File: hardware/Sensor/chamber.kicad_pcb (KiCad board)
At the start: 2 copper layers, 100 x 100 mm, 99 parts, among them J1 USB_B_Micro, J32 RF_Shield_Two_Pieces, J33 RF_Shield_Two_Pieces, J34 Conn_Coaxial, J51 Conn_02x05_Counter_Clockwise, J52 Conn_01x04, Q31 BC859, Q32 Q_NMOS_GDS, Q51 2N7002, Q52 Q_NPN_BEC, SW31 SW_DPDT_x2, SW32 SW_DPDT_x2, U31 MC34063AD, U32 LMC662, U33 LM358, U51 Opamp_Dual_Generic, U52 MCP3425A0T-ECH, U53 MCP3425A0T-ECH, U54 STM8S003F3P

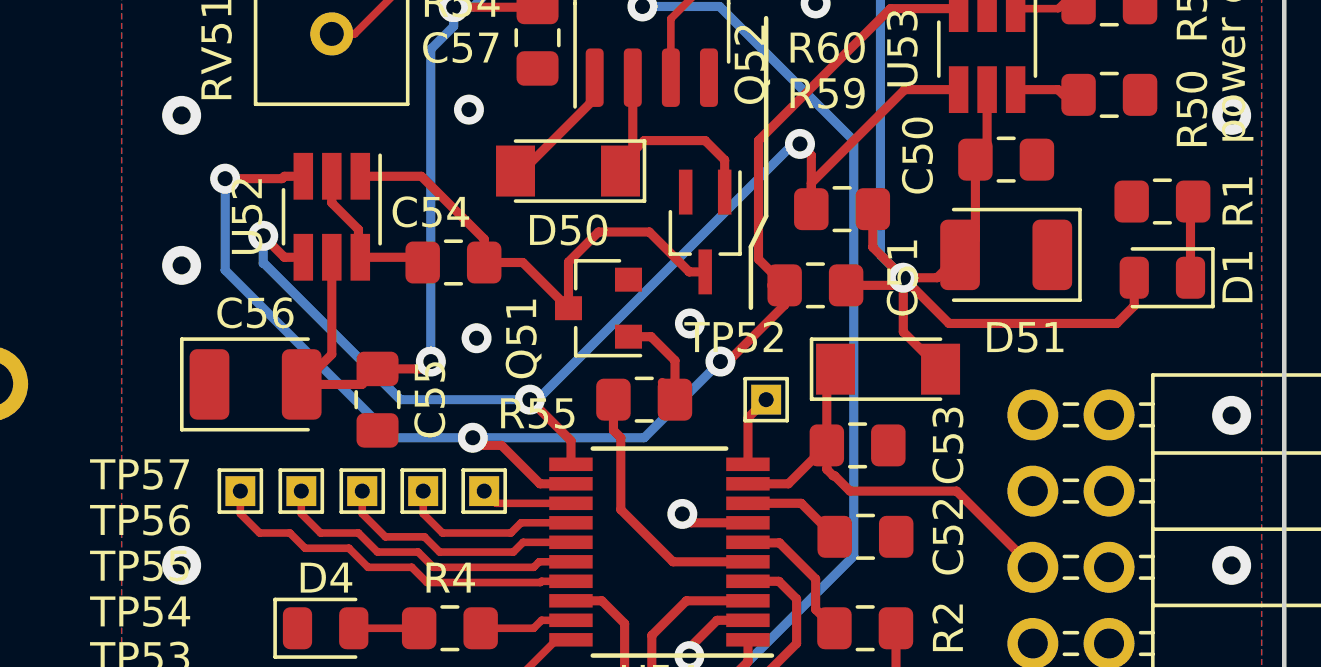
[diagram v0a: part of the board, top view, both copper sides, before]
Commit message: fix #56 #74
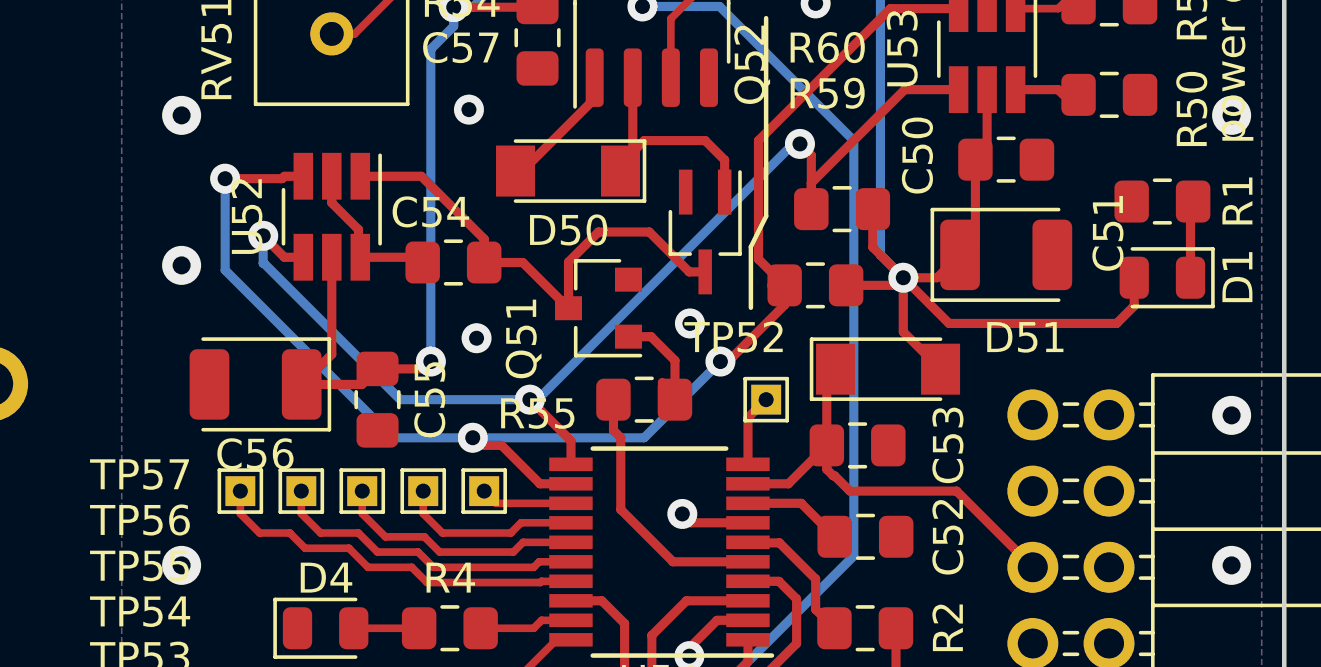
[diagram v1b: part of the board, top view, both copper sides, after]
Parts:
- C51, C56: value 10n -> 10u
- turned C51 to 0 degrees
- turned C56 to 180 degrees
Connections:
- C51 pad 1: GND -> VCC_5V
- C51 pad 2: VCC_5V -> GND
- C56 pad 1: GND -> VCC_5V
- C56 pad 2: VCC_5V -> GND
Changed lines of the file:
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@@
   (page A4)
   (layers
-    (0 F.Cu signal hide)
-    (31 B.Cu signal hide)
+    (0 F.Cu signal)
+    (31 B.Cu signal)
     (32 B.Adhes user)
     (33 F.Adhes user)
@@
   )
   (module Capacitor_Tantalum_SMD:CP_EIA-3528-21_Kemet-B (layer F.Cu)
-    (at 172.466 123.968)
+    (at 172.466 123.968 180)
     (descr "Tantalum Capacitor SMD Kemet-B (3528-21 Metric), IPC_7351 nominal, (Body size from: http://www.kemet.com/Lists/ProductCatalog/Attachments/253/KEM_TC101_STD.pdf), generated with kicad-footprint-generator")
     (tags "capacitor tantalum")
@@
       (effects (font (size 1 1) (thickness 0.15)))
     )
-    (fp_text value 10n (at 0 2.35) (layer F.Fab)
-      (effects (font (size 1 1) (thickness 0.15)))
-    )
-    (fp_text user %R (at 0 0) (layer F.Fab)
+    (fp_text value 10u (at 0 2.35) (layer F.Fab)
+      (effects (font (size 1 1) (thickness 0.15)))
+    )
+    (fp_text user %R (at 0 0) (layer F.Fab)
+      (effects (font (size 0.88 0.88) (thickness 0.13)))
+    )
+    (fp_line (start 2.45 1.65) (end -2.45 1.65) (layer F.CrtYd) (width 0.05))
+    (fp_line (start 2.45 -1.65) (end 2.45 1.65) (layer F.CrtYd) (width 0.05))
+    (fp_line (start -2.45 -1.65) (end 2.45 -1.65) (layer F.CrtYd) (width 0.05))
+    (fp_line (start -2.45 1.65) (end -2.45 -1.65) (layer F.CrtYd) (width 0.05))
+    (fp_line (start -2.46 1.51) (end 1.75 1.51) (layer F.SilkS) (width 0.12))
+    (fp_line (start -2.46 -1.51) (end -2.46 1.51) (layer F.SilkS) (width 0.12))
+    (fp_line (start 1.75 -1.51) (end -2.46 -1.51) (layer F.SilkS) (width 0.12))
+    (fp_line (start 1.75 1.4) (end 1.75 -1.4) (layer F.Fab) (width 0.1))
+    (fp_line (start -1.75 1.4) (end 1.75 1.4) (layer F.Fab) (width 0.1))
+    (fp_line (start -1.75 -0.7) (end -1.75 1.4) (layer F.Fab) (width 0.1))
+    (fp_line (start -1.05 -1.4) (end -1.75 -0.7) (layer F.Fab) (width 0.1))
+    (fp_line (start 1.75 -1.4) (end -1.05 -1.4) (layer F.Fab) (width 0.1))
+    (pad 2 smd roundrect (at 1.5375 0 180) (size 1.325 2.35) (layers F.Cu F.Paste F.Mask) (roundrect_rratio 0.188679)
+      (net 1 GND))
+    (pad 1 smd roundrect (at -1.5375 0 180) (size 1.325 2.35) (layers F.Cu F.Paste F.Mask) (roundrect_rratio 0.188679)
+      (net 47 VCC_5V))
+    (model ${KISYS3DMOD}/Capacitor_Tantalum_SMD.3dshapes/CP_EIA-3528-21_Kemet-B.wrl
+      (at (xyz 0 0 0))
+      (scale (xyz 1 1 1))
+      (rotate (xyz 0 0 0))
+    )
+  )
+  (module Capacitor_Tantalum_SMD:CP_EIA-3528-21_Kemet-B (layer F.Cu)
+    (at 197.485 119.65)
+    (descr "Tantalum Capacitor SMD Kemet-B (3528-21 Metric), IPC_7351 nominal, (Body size from: http://www.kemet.com/Lists/ProductCatalog/Attachments/253/KEM_TC101_STD.pdf), generated with kicad-footprint-generator")
+    (tags "capacitor tantalum")
+    (attr smd)
+    (fp_text reference C51 (at 3.429 -0.746 270) (layer F.SilkS)
+      (effects (font (size 1 1) (thickness 0.15)))
+    )
+    (fp_text value 10u (at 0 2.35 180) (layer F.Fab)
+      (effects (font (size 1 1) (thickness 0.15)))
+    )
+    (fp_text user %R (at 0 0 180) (layer F.Fab)
       (effects (font (size 0.88 0.88) (thickness 0.13)))
     )
@@
     (fp_line (start 1.75 -1.4) (end -1.05 -1.4) (layer F.Fab) (width 0.1))
     (pad 2 smd roundrect (at 1.5375 0) (size 1.325 2.35) (layers F.Cu F.Paste F.Mask) (roundrect_rratio 0.188679)
+      (net 1 GND))
+    (pad 1 smd roundrect (at -1.5375 0) (size 1.325 2.35) (layers F.Cu F.Paste F.Mask) (roundrect_rratio 0.188679)
       (net 47 VCC_5V))
-    (pad 1 smd roundrect (at -1.5375 0) (size 1.325 2.35) (layers F.Cu F.Paste F.Mask) (roundrect_rratio 0.188679)
-      (net 1 GND))
     (model ${KISYS3DMOD}/Capacitor_Tantalum_SMD.3dshapes/CP_EIA-3528-21_Kemet-B.wrl
       (at (xyz 0 0 0))
-      (scale (xyz 1 1 1))
-      (rotate (xyz 0 0 0))
-    )
-  )
-  (module Capacitor_Tantalum_SMD:CP_EIA-3528-21_Kemet-B (layer F.Cu)
-    (at 197.485 119.65 180)
-    (descr "Tantalum Capacitor SMD Kemet-B (3528-21 Metric), IPC_7351 nominal, (Body size from: http://www.kemet.com/Lists/ProductCatalog/Attachments/253/KEM_TC101_STD.pdf), generated with kicad-footprint-generator")
-    (tags "capacitor tantalum")
-    (attr smd)
-    (fp_text reference C51 (at 3.429 -0.746 270) (layer F.SilkS)
-      (effects (font (size 1 1) (thickness 0.15)))
-    )
-    (fp_text value 10n (at 0 2.35 180) (layer F.Fab)
-      (effects (font (size 1 1) (thickness 0.15)))
-    )
-    (fp_text user %R (at 0 0 180) (layer F.Fab)
-      (effects (font (size 0.88 0.88) (thickness 0.13)))
-    )
-    (fp_line (start 2.45 1.65) (end -2.45 1.65) (layer F.CrtYd) (width 0.05))
-    (fp_line (start 2.45 -1.65) (end 2.45 1.65) (layer F.CrtYd) (width 0.05))
-    (fp_line (start -2.45 -1.65) (end 2.45 -1.65) (layer F.CrtYd) (width 0.05))
-    (fp_line (start -2.45 1.65) (end -2.45 -1.65) (layer F.CrtYd) (width 0.05))
-    (fp_line (start -2.46 1.51) (end 1.75 1.51) (layer F.SilkS) (width 0.12))
-    (fp_line (start -2.46 -1.51) (end -2.46 1.51) (layer F.SilkS) (width 0.12))
-    (fp_line (start 1.75 -1.51) (end -2.46 -1.51) (layer F.SilkS) (width 0.12))
-    (fp_line (start 1.75 1.4) (end 1.75 -1.4) (layer F.Fab) (width 0.1))
-    (fp_line (start -1.75 1.4) (end 1.75 1.4) (layer F.Fab) (width 0.1))
-    (fp_line (start -1.75 -0.7) (end -1.75 1.4) (layer F.Fab) (width 0.1))
-    (fp_line (start -1.05 -1.4) (end -1.75 -0.7) (layer F.Fab) (width 0.1))
-    (fp_line (start 1.75 -1.4) (end -1.05 -1.4) (layer F.Fab) (width 0.1))
-    (pad 2 smd roundrect (at 1.5375 0 180) (size 1.325 2.35) (layers F.Cu F.Paste F.Mask) (roundrect_rratio 0.188679)
-      (net 47 VCC_5V))
-    (pad 1 smd roundrect (at -1.5375 0 180) (size 1.325 2.35) (layers F.Cu F.Paste F.Mask) (roundrect_rratio 0.188679)
-      (net 1 GND))
-    (model ${KISYS3DMOD}/Capacitor_Tantalum_SMD.3dshapes/CP_EIA-3528-21_Kemet-B.wrl
-      (at (xyz 0 0 0))

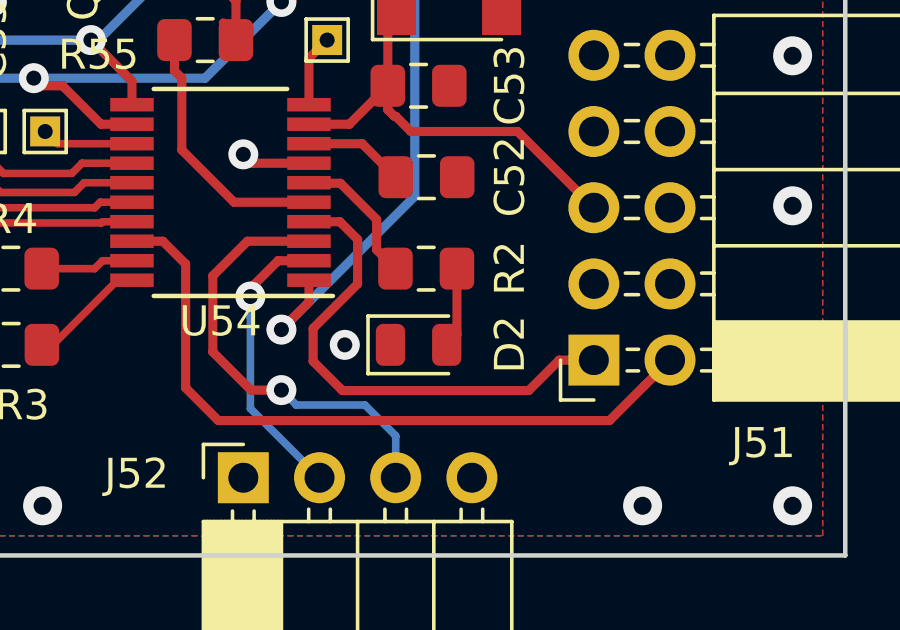
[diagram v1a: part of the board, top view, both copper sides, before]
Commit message: fix #59 #71
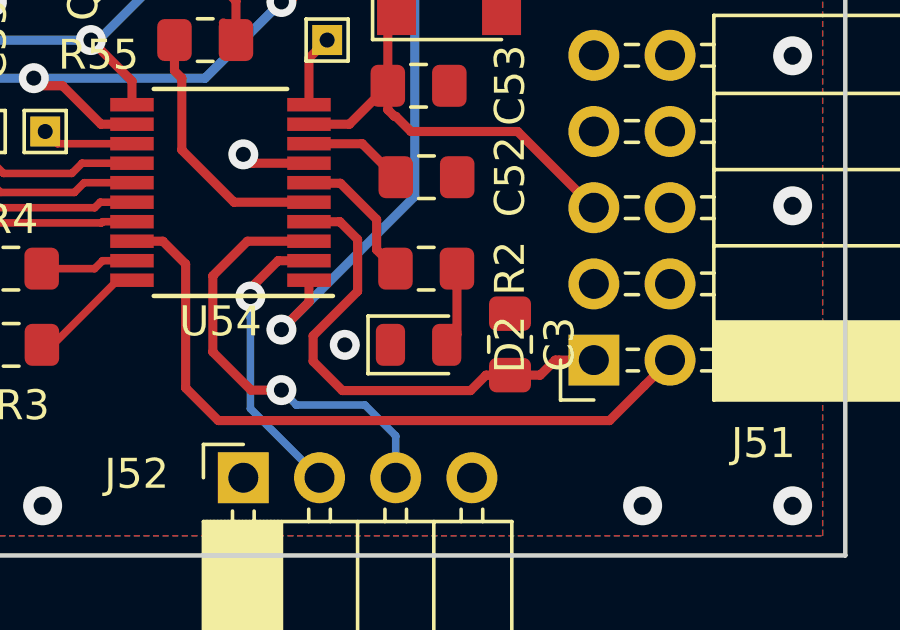
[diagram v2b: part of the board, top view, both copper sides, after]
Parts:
- added C3: 10n, Capacitor_SMD:C_0805_2012Metric_Pad1.15x1.40mm_HandSolder, F.Cu at (195.6, 134.6)
- C32: value 3n2 -> 3n3
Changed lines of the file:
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@@
     (thickness 1.6)
     (drawings 19)
-    (tracks 661)
+    (tracks 665)
     (zones 0)
-    (modules 99)
+    (modules 100)
     (nets 66)
   )
@@
     (add_net "Net-(R37-Pad1)")
   )
+  (module Capacitor_SMD:C_0805_2012Metric_Pad1.15x1.40mm_HandSolder (layer F.Cu)
+    (at 195.58 134.62 270)
+    (descr "Capacitor SMD 0805 (2012 Metric), square (rectangular) end terminal, IPC_7351 nominal with elongated pad for handsoldering. (Body size source: https://docs.google.com/spreadsheets/d/1BsfQQcO9C6DZCsRaXUlFlo91Tg2WpOkGARC1WS5S8t0/edit?usp=sharing), generated with kicad-footprint-generator")
+    (tags "capacitor handsolder")
+    (attr smd)
+    (fp_text reference C3 (at 0 -1.65 90) (layer F.SilkS)
+      (effects (font (size 1 1) (thickness 0.15)))
+    )
+    (fp_text value 10n (at 0 1.65 90) (layer F.Fab)
+      (effects (font (size 1 1) (thickness 0.15)))
+    )
+    (fp_text user %R (at 0 0 90) (layer F.Fab)
+      (effects (font (size 0.5 0.5) (thickness 0.08)))
+    )
+    (fp_line (start 1.85 0.95) (end -1.85 0.95) (layer F.CrtYd) (width 0.05))
+    (fp_line (start 1.85 -0.95) (end 1.85 0.95) (layer F.CrtYd) (width 0.05))
+    (fp_line (start -1.85 -0.95) (end 1.85 -0.95) (layer F.CrtYd) (width 0.05))
+    (fp_line (start -1.85 0.95) (end -1.85 -0.95) (layer F.CrtYd) (width 0.05))
+    (fp_line (start -0.261252 0.71) (end 0.261252 0.71) (layer F.SilkS) (width 0.12))
+    (fp_line (start -0.261252 -0.71) (end 0.261252 -0.71) (layer F.SilkS) (width 0.12))
+    (fp_line (start 1 0.6) (end -1 0.6) (layer F.Fab) (width 0.1))
+    (fp_line (start 1 -0.6) (end 1 0.6) (layer F.Fab) (width 0.1))
+    (fp_line (start -1 -0.6) (end 1 -0.6) (layer F.Fab) (width 0.1))
+    (fp_line (start -1 0.6) (end -1 -0.6) (layer F.Fab) (width 0.1))
+    (pad 2 smd roundrect (at 1.025 0 270) (size 1.15 1.4) (layers F.Cu F.Paste F.Mask) (roundrect_rratio 0.217391)
+      (net 45 /DataAcquisition/RST))
+    (pad 1 smd roundrect (at -1.025 0 270) (size 1.15 1.4) (layers F.Cu F.Paste F.Mask) (roundrect_rratio 0.217391)
+      (net 1 GND))
+    (model ${KISYS3DMOD}/Capacitor_SMD.3dshapes/C_0805_2012Metric.wrl
+      (at (xyz 0 0 0))
+      (scale (xyz 1 1 1))
+      (rotate (xyz 0 0 0))
+    )
+  )
   (module IonizationChamber:SwitchButtonGeneric (layer F.Cu)
     (at 163.195 101.6)
@@
       (effects (font (size 1 1) (thickness 0.15)))
     )
-    (fp_text value 3n2 (at 0 1.65) (layer F.Fab)
+    (fp_text value 3n3 (at 0 1.65) (layer F.Fab)
       (effects (font (size 1 1) (thickness 0.15)))
     )
@@
   (segment (start 184.767598 136.071074) (end 185.856524 137.16) (width 0.3048) (layer F.Cu) (net 44))
   (segment (start 185.856524 137.16) (end 198.898 137.16) (width 0.3048) (layer F.Cu) (net 44))
-  (segment (start 189.016401 135.184401) (end 189.992 136.16) (width 0.3048) (layer F.Cu) (net 45))
-  (segment (start 189.016401 134.087599) (end 189.016401 135.184401) (width 0.3048) (layer F.Cu) (net 45))
-  (segment (start 190.5 132.604) (end 189.016401 134.087599) (width 0.3048) (layer F.Cu) (net 45))
-  (segment (start 190.5 131.121478) (end 190.5 132.604) (width 0.3048) (layer F.Cu) (net 45))
-  (segment (start 188.878 130.531) (end 189.909522 130.531) (width 0.3048) (layer F.Cu) (net 45) (status 10))
-  (segment (start 189.909522 130.531) (end 190.5 131.121478) (width 0.3048) (layer F.Cu) (net 45))
-  (segment (start 189.992 136.16) (end 196.2032 136.16) (width 0.3048) (layer F.Cu) (net 45))
-  (segment (start 196.2032 136.16) (end 197.2192 135.144) (width 0.3048) (layer F.Cu) (net 45))
   (segment (start 197.2192 135.144) (end 198.374 135.144) (width 0.3048) (layer F.Cu) (net 45) (status 20))
+  (segment (start 195.58 135.645) (end 196.587 135.645) (width 0.3048) (layer F.Cu) (net 45))
+  (segment (start 197.088 135.144) (end 197.2192 135.144) (width 0.3048) (layer F.Cu) (net 45))
+  (segment (start 196.587 135.645) (end 197.088 135.144) (width 0.3048) (layer F.Cu) (net 45))
+  (segment (start 194.265 136.16) (end 194.78 135.645) (width 0.3048) (layer F.Cu) (net 45))
+  (segment (start 189.992 136.16) (end 194.265 136.16) (width 0.3048) (layer F.Cu) (net 45))
+  (segment (start 194.78 135.645) (end 195.58 135.645) (width 0.3048) (layer F.Cu) (net 45))
+  (segment (start 188.878 130.531) (end 189.909522 130.531) (width 0.3048) (layer F.Cu) (net 45))
+  (segment (start 190.5 131.121478) (end 190.5 132.85) (width 0.3048) (layer F.Cu) (net 45))
+  (segment (start 190.5 132.85) (end 189.016401 134.333599) (width 0.3048) (layer F.Cu) (net 45))
+  (segment (start 189.016401 134.333599) (end 189.016401 135.184401) (width 0.3048) (layer F.Cu) (net 45))
+  (segment (start 189.909522 130.531) (end 190.5 131.121478) (width 0.3048) (layer F.Cu) (net 45))
+  (segment (start 189.016401 135.184401) (end 189.992 136.16) (width 0.3048) (layer F.Cu) (net 45))
   (segment (start 195.834 127.524) (end 198.374 130.064) (width 0.3048) (layer F.Cu) (net 46) (status 20))
   (segment (start 191.77 127.016) (end 192.278 127.524) (width 0.3048) (layer F.Cu) (net 46))

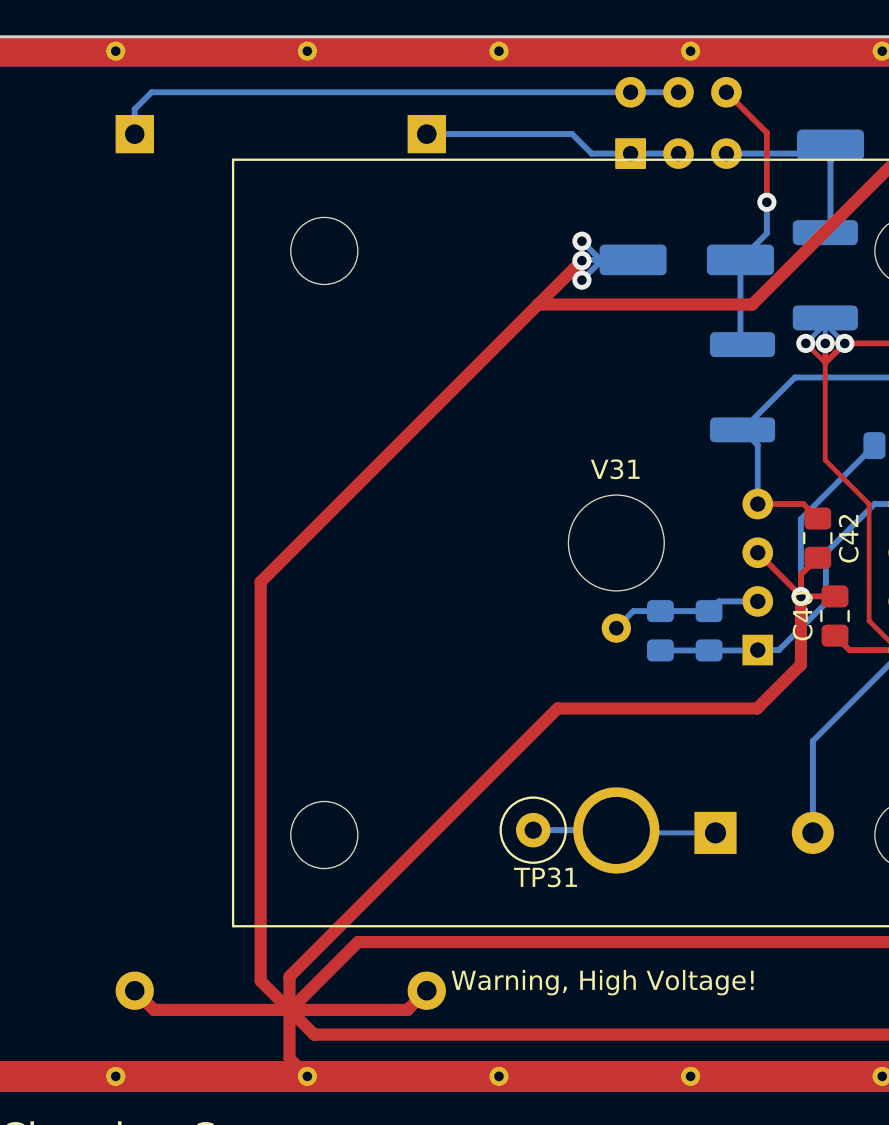
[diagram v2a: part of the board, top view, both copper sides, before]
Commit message: fix #196
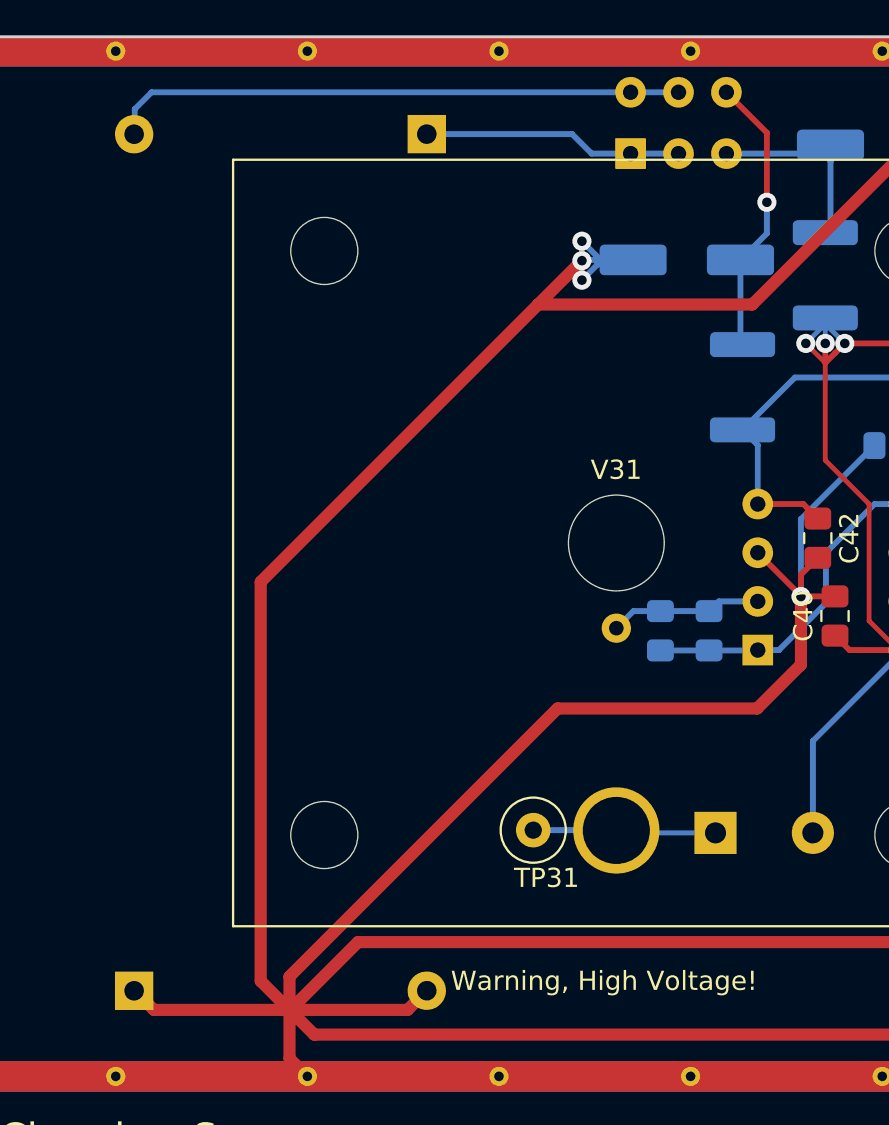
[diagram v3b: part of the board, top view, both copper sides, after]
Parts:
- moved BT32 44.7 mm to (129.5, 91.4), turned to 90 degrees
- turned C34 to 0 degrees
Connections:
- BT32 pad 1: Net-(BT32-Pad1) -> GND
- BT32 pad 2: GND -> Net-(BT32-Pad2)
- C34 pad 1: Net-(C34-Pad1) -> GND
- C34 pad 2: GND -> Net-(C34-Pad2)
- L33 pad 2: Net-(C34-Pad1) -> Net-(C34-Pad2)
- SW31 pad 4: Net-(BT32-Pad1) -> Net-(BT32-Pad2)
- SW31 pad 5: Net-(BT32-Pad1) -> Net-(BT32-Pad2)
- SW31 pad 6: Net-(C34-Pad1) -> Net-(C34-Pad2)
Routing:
- net Net-(BT32-Pad2): track 0.00 -> 30.0 mm
- net Net-(BT32-Pad1): track 30.0 -> 0.00 mm
- net Net-(C34-Pad2): track 0.00 -> 14.7 mm, vias 0 -> 1
- net Net-(C34-Pad1): track 14.7 -> 0.00 mm, vias 1 -> 0
